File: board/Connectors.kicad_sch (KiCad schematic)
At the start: 17 parts, among them J10 SLOT 4, J11 SLOT 1, J12 SLOT 5, J13 SLOT 2, J14 SPI Device 0, J15 SPI Device 4, J16 SPI Device 1, J17 SPI Device 5, J18 Audio Jack, J19 SPI Device 2, J20 SPI Device 6, J21 SPI Device 3, J22 SPI Device 7, J23 SLOT 3, J24 VIA Port A, J25 SP720APP, J9 SLOT 0

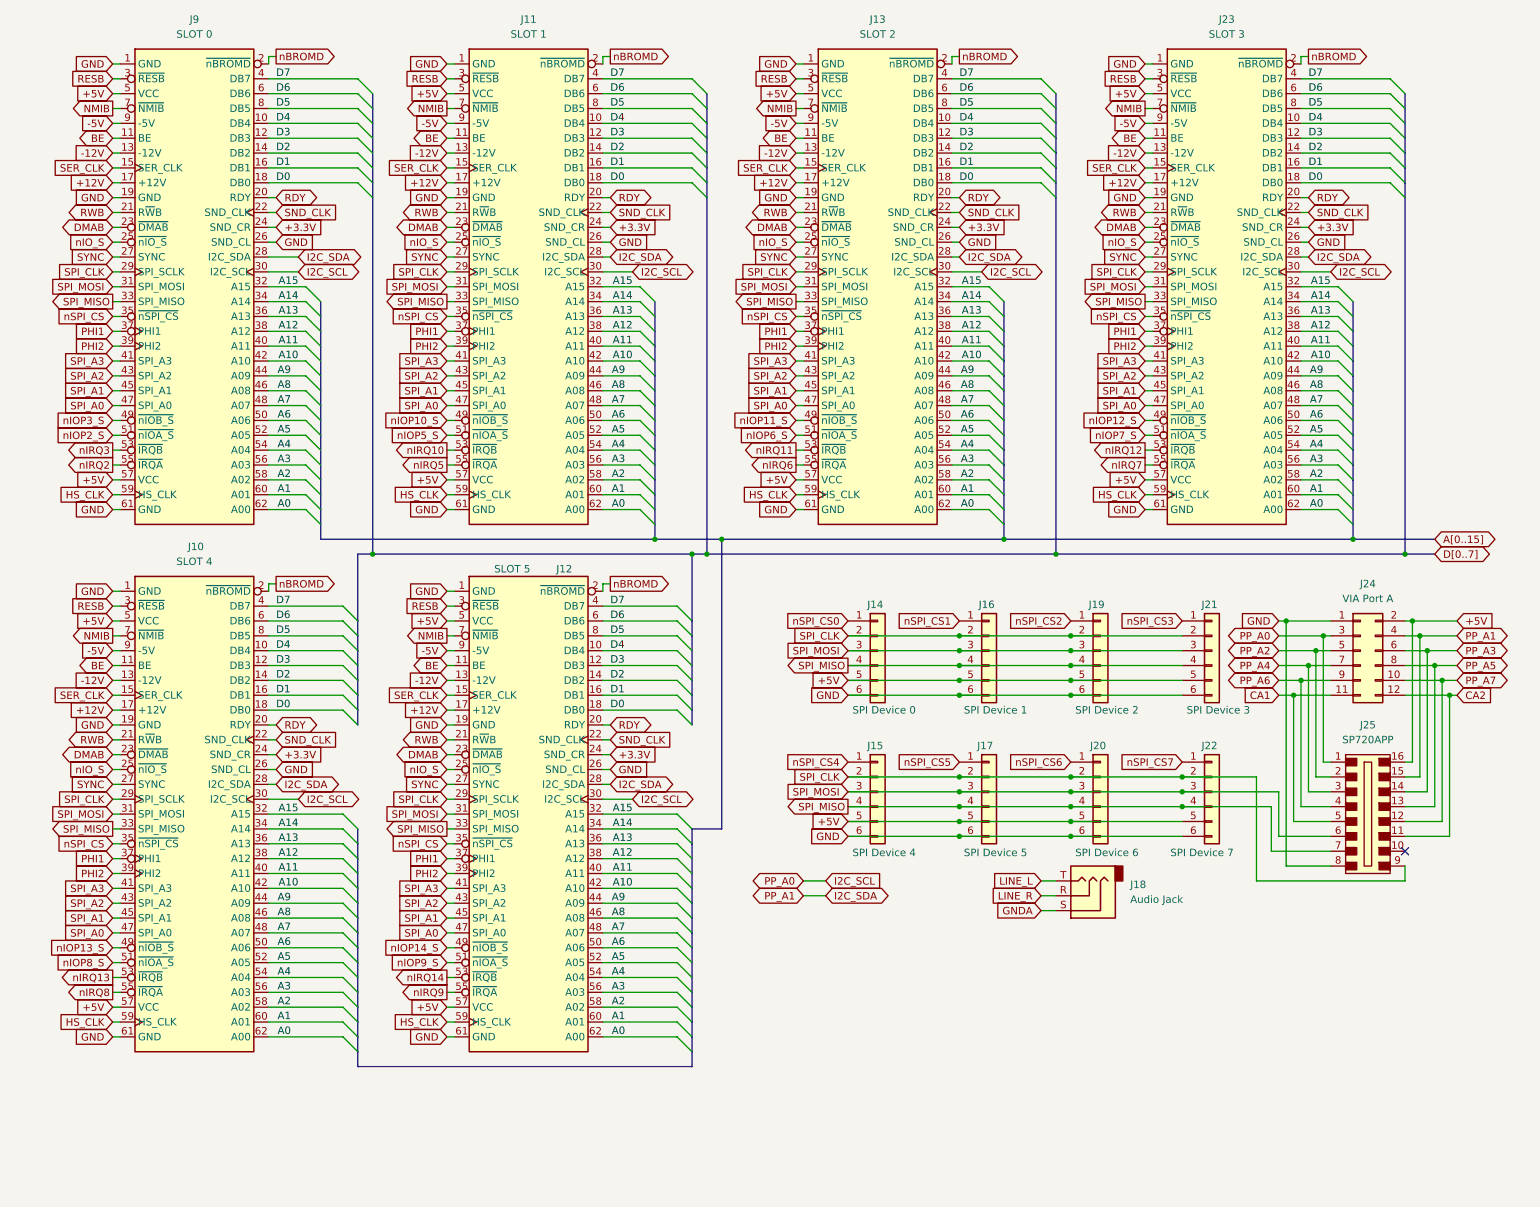
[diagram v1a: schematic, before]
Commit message: V2.0 rev 2.0D: clock stretching, OS ROM paging and review fixes
Bus timing:
- New GAL C (U88) generates PHI2/PHI1 and the 3.58 MHz sound clock from
  the 14.318 MHz master, replacing the U35 74F191 divider. J36 now selects
  7.16 or 3.58 MHz.
- Banked RAM, banked ROM and slot I/O ($FF20-$FFEF) get one extra PHI2-low
  period plus 0-3 extra PHI2-high periods set in $FFF5 (GAL D). This
  replaces the on-board RDY wait generator; cards can still pull RDY.
- Write strobes are now hold-time safe: PHI1 comes straight from GAL C
  and RWB_M straight from GAL B2.

Review fixes:
- OS ROM chip enable from a single-level decode, output enable from
  GAL B1; -55 part specified. Full 4K OS ROM paging via GAL G.
- Vector RAM writes only during PHI2; $FFF0-$FFFF no longer slowed.
- YM2151 /WR on RWB_M. U62 removed. RB0-RB7 pull-ups (RN5).
- Slot clocks driven through U56 and U34 with 33R series resistors.
- J38 enables in-system flashing of the banked ROMs.
- W65C22S/W65C51N, AS6C4008, DS1813-5 and CY7C192-25 values; R4 1k.
- J7 pin 8 no longer +5V; +5VA renamed +5VSB; serial handshake loop.
- Sheet titles and revisions, slot symbol pin fixes, and project symbol
  and footprint libraries so the project opens on another machine.

Co-Authored-By: Claude Opus 5.5 <noreply@anthropic.com>
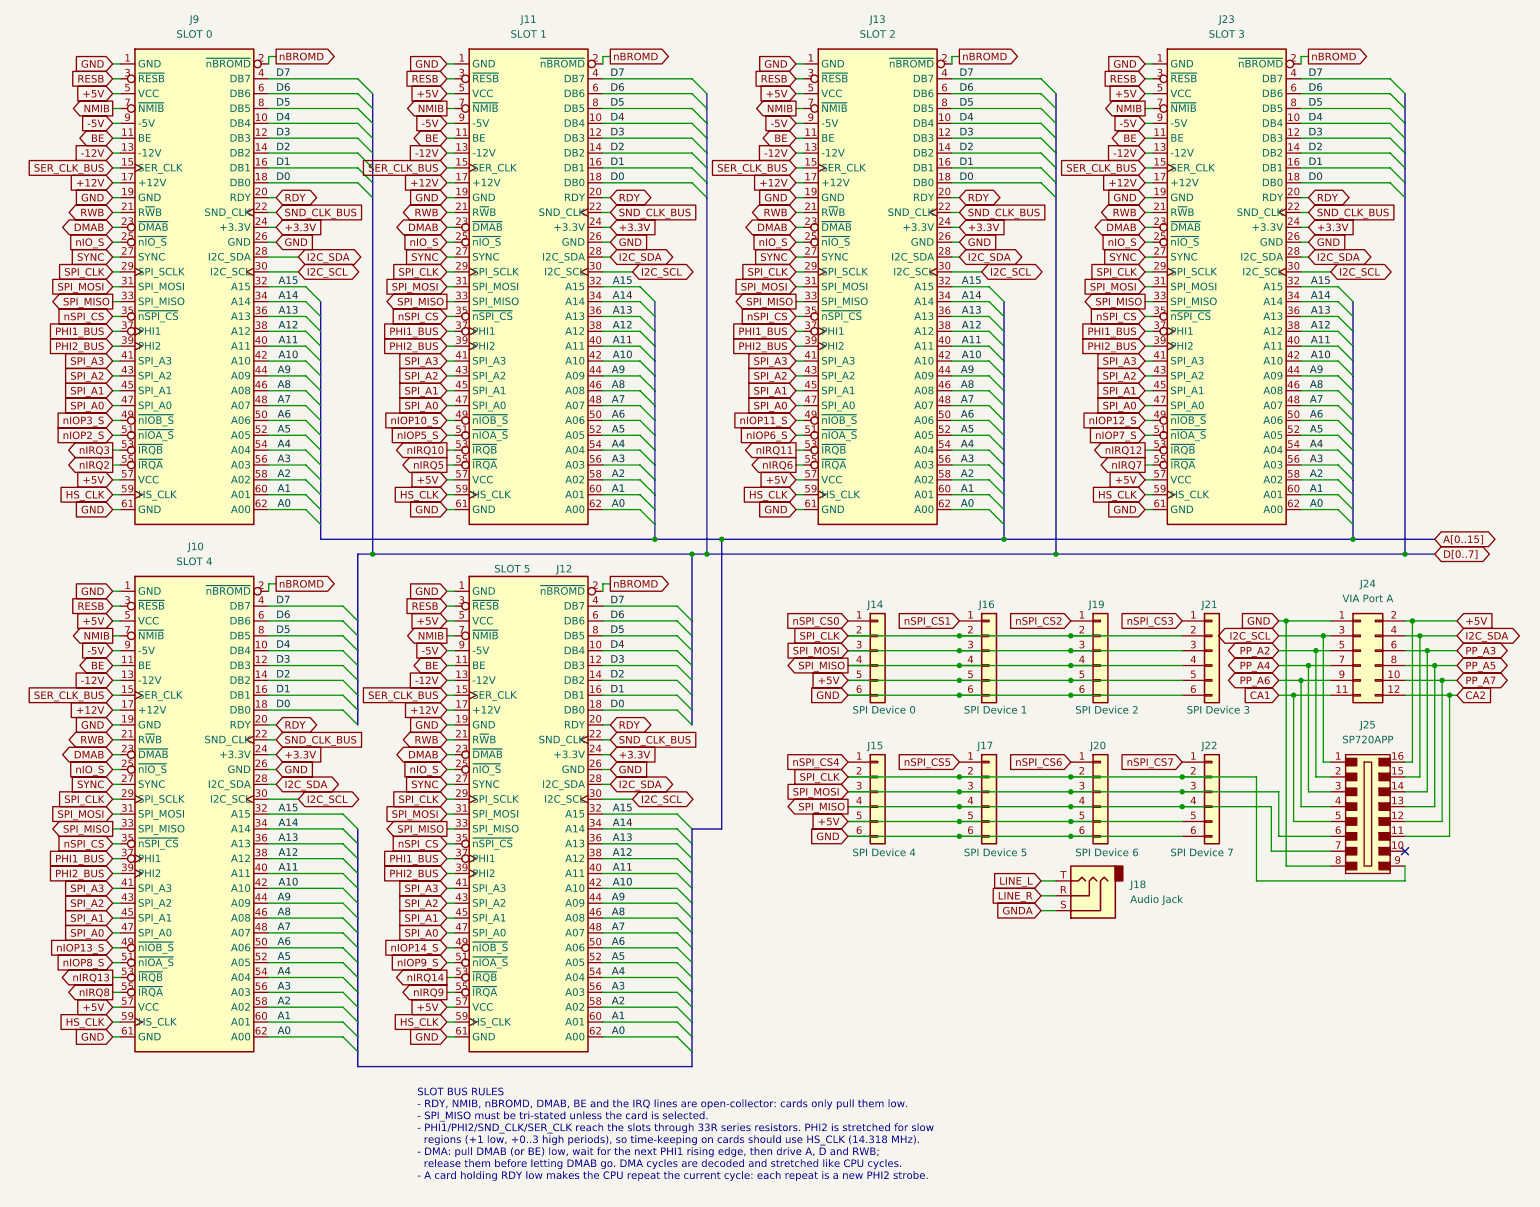
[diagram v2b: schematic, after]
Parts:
- J10, J11, J12, J13, J23, J9: footprint PC Edge:TE_7-5530843-0 -> Hydra16:TE_7-5530843-0; symbol Connector:Bus_Hydra_8bit -> Hydra16:Bus_Hydra_8bit
- J25: symbol dk_Sockets-for-ICs-Transistors:A_16-LC-TT -> Hydra16:A_16-LC-TT
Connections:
- net PHI1 renamed PHI1_BUS
- net PHI2 renamed PHI2_BUS
- net SER_CLK renamed SER_CLK_BUS
- net SND_CLK renamed SND_CLK_BUS
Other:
- note added: "SLOT BUS RULES - RDY, NMIB, nBROMD, DMAB, BE and the IRQ lines are open-collector: cards only pull them low. - SPI_MISO must be tri-stated unless the card is selected. - PHI1/PHI2/SND_CLK/SER_CLK reach the slots through 33R series resistors. PHI2 is stretched for slow regions (+1 low, +0..3 high periods), so time-keeping on cards should use HS_CLK (14.318 MHz). - DMA: pull DMAB (or BE) low, wait 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"
- title: ZeroPage $00/$01 Mirror Memory and RAM/ROM Bank Logic -> Expansion Slots, SPI Headers and Port A
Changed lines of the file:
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@@
 	(generator "eeschema")
 	(generator_version "9.0")
-	(paper "USLetter")
+	(paper "USLedger")
 	(title_block
-		(title "ZeroPage $00/$01 Mirror Memory and RAM/ROM Bank Logic")
-		(date "2026-01-28")
-		(rev "2.0B")
+		(title "Expansion Slots, SPI Headers and Port A")
+		(date "2026-10-06")
+		(rev "2.0D")
 		(company "Data Tuning")
 		(comment 1 "Hydra 16")
@@
 	(wire
 		(pts
-			(xy 144.78 165.1) (xy 148.59 165.1)
-		)
-		(stroke
-			(width 0)
-			(type default)
-		)
-	)
-	(wire
-		(pts
 			(xy 229.87 71.12) (xy 236.22 71.12)
 		)
@@
 	(wire
 		(pts
-			(xy 144.78 162.56) (xy 148.59 162.56)
-		)
-		(stroke
-			(width 0)
-			(type default)
-		)
-	)
-	(wire
-		(pts
 			(xy 83.82 115.57) (xy 85.09 115.57)
 		)
@@
 		)
 	)
-	(global_label "SER_CLK"
+	(global_label "SER_CLK_BUS"
 		(shape input)
 		(at 26.67 130.81 180)
@@
 		)
 	)
-	(global_label "PP_A1"
-		(shape bidirectional)
-		(at 144.78 165.1 180)
-		(fields_autoplaced yes)
-		(effects
-			(font
-				(size 1.27 1.27)
-			)
-			(justify right)
-		)
-		(property "Intersheetrefs" "${INTERSHEET_REFS}"
-			(at 134.8778 165.1 0)
-			(effects
-				(font
-					(size 1.27 1.27)
-				)
-				(justify right)
-				(hide yes)
-			)
-		)
-	)
 	(global_label "nIO_S"
 		(shape input)
@@
 		)
 	)
-	(global_label "SND_CLK"
+	(global_label "SND_CLK_BUS"
 		(shape input)
 		(at 54.61 138.43 0)
@@
 		)
 	)
-	(global_label "PHI1"
+	(global_label "PHI1_BUS"
 		(shape input)
 		(at 143.51 68.58 180)
@@
 		)
 	)
-	(global_label "SND_CLK"
+	(global_label "SND_CLK_BUS"
 		(shape input)
 		(at 171.45 48.26 0)
@@
 		)
 	)
-	(global_label "SER_CLK"
+	(global_label "SER_CLK_BUS"
 		(shape input)
 		(at 143.51 40.64 180)
@@
 		)
 	)
-	(global_label "SER_CLK"
+	(global_label "SER_CLK_BUS"
 		(shape input)
 		(at 203.2 40.64 180)
@@
 		)
 	)
-	(global_label "PHI2"
+	(global_label "PHI2_BUS"
 		(shape input)
 		(at 83.82 71.12 180)
@@
 		)
 	)
-	(global_label "PHI2"
+	(global_label "PHI2_BUS"
 		(shape input)
 		(at 83.82 161.29 180)
@@
 		)
 	)
-	(global_label "PHI2"
+	(global_label "PHI2_BUS"
 		(shape input)
 		(at 143.51 71.12 180)
@@
 		)
 	)
-	(global_label "SER_CLK"
+	(global_label "SER_CLK_BUS"
 		(shape input)
 		(at 26.67 40.64 180)
@@
 		)
 	)
-	(global_label "PHI1"
+	(global_label "PHI1_BUS"
 		(shape input)
 		(at 83.82 68.58 180)
@@
 		)
 	)
-	(global_label "SND_CLK"
+	(global_label "SND_CLK_BUS"
 		(shape input)
 		(at 231.14 48.26 0)
@@
 		)
 	)
-	(global_label "SND_CLK"
+	(global_label "SND_CLK_BUS"
 		(shape input)
 		(at 111.76 138.43 0)
@@
 		)
 	)
-	(global_label "PHI2"
+	(global_label "PHI2_BUS"
 		(shape input)
 		(at 203.2 71.12 180)
@@
 		)
 	)
-	(global_label "PHI1"
+	(global_label "PHI1_BUS"
 		(shape input)
 		(at 26.67 68.58 180)
@@
 		)
 	)
-	(global_label "PHI2"
+	(global_label "PHI2_BUS"
 		(shape input)
 		(at 26.67 161.29 180)
@@
 		)
 	)
-	(global_label "PP_A0"
+	(global_label "I2C_SCL"
 		(shape bidirectional)
 		(at 226.06 120.65 180)
@@
 		)
 	)
-	(global_label "PHI1"
+	(global_label "PHI1_BUS"
 		(shape input)
 		(at 203.2 68.58 180)
@@
 		)
 	)
-	(global_label "PHI2"
+	(global_label "PHI2_BUS"
 		(shape input)
 		(at 26.67 71.12 180)
@@
 		)
 	)
-	(global_label "PHI1"
+	(global_label "PHI1_BUS"
 		(shape input)
 		(at 26.67 158.75 180)
@@
 		)
 	)
-	(global_label "PP_A0"
-		(shape bidirectional)
-		(at 144.78 162.56 180)
-		(fields_autoplaced yes)
-		(effects
-			(font
-				(size 1.27 1.27)
-			)
-			(justify right)
-		)
-		(property "Intersheetrefs" "${INTERSHEET_REFS}"
-			(at 134.8778 162.56 0)
-			(effects
-				(font
-					(size 1.27 1.27)
-				)
-				(justify right)
-				(hide yes)
-			)
-		)
-	)
 	(global_label "SPI_CLK"
 		(shape input)
@@
 		)
 	)
-	(global_label "I2C_SDA"
-		(shape bidirectional)
-		(at 148.59 165.1 0)
-		(fields_autoplaced yes)
-		(effects
-			(font
-				(size 1.27 1.27)
-			)
-			(justify left)
-		)
-		(property "Intersheetrefs" "${INTERSHEET_REFS}"
-			(at 160.3065 165.1 0)
-			(effects
-				(font
-					(size 1.27 1.27)
-				)
-				(justify left)
-				(hide yes)
-			)
-		)
-	)
 	(global_label "nIOP13_S"
 		(shape input)
@@
 		)
 	)
-	(global_label "SND_CLK"
+	(global_label "SND_CLK_BUS"
 		(shape input)
 		(at 111.76 48.26 0)
@@
 		)
 	)
-	(global_label "PP_A1"
+	(global_label "I2C_SDA"
 		(shape bidirectional)
 		(at 256.54 120.65 0)
@@
 		)
 	)
-	(global_label "SER_CLK"
+	(global_label "SER_CLK_BUS"
 		(shape input)
 		(at 83.82 130.81 180)
@@
 		)
 	)
-	(global_label "SER_CLK"
+	(global_label "SER_CLK_BUS"
 		(shape input)
 		(at 83.82 40.64 180)
@@
 		)
 	)
-	(global_label "SND_CLK"
+	(global_label "SND_CLK_BUS"
 		(shape input)
 		(at 54.61 48.26 0)
@@
 		)
 	)
-	(global_label "PHI1"
+	(global_label "PHI1_BUS"
 		(shape input)
 		(at 83.82 158.75 180)
@@
 		)
 	)
-	(global_label "I2C_SCL"
-		(shape input)
-		(at 148.59 162.56 0)
-		(fields_autoplaced yes)
-		(effects
-			(font
-				(size 1.27 1.27)
-			)
-			(justify left)
-		)
-		(property "Intersheetrefs" "${INTERSHEET_REFS}"
-			(at 159.1347 162.56 0)
-			(effects
-				(font
-					(size 1.27 1.27)
-				)
-				(justify left)
-				(hide yes)
-			)
-		)
-	)
 	(global_label "SPI_A3"
 		(shape input)
@@
 	)
 	(symbol
-		(lib_id "Connector:Bus_Hydra_8bit")
+		(lib_id "Hydra16:Bus_Hydra_8bit")
 		(at 97.79 60.96 0)
 		(unit 1)
@@
 			)
 		)
-		(property "Footprint" "PC Edge:TE_7-5530843-0"
+		(property "Footprint" "Hydra16:TE_7-5530843-0"
 			(at 97.79 105.918 0)
 			(effects
@@
 	)
 	(symbol
-		(lib_name "Bus_Hydra_8bit_3")
-		(lib_id "Connector:Bus_Hydra_8bit")
+		(lib_id "Hydra16:Bus_Hydra_8bit")
 		(at 40.64 151.13 0)
 		(unit 1)
@@
 			)
 		)
-		(property "Footprint" "PC Edge:TE_7-5530843-0"
+		(property "Footprint" "Hydra16:TE_7-5530843-0"
 			(at 40.64 196.088 0)
 			(effects
@@
 	)
 	(symbol
-		(lib_name "Bus_Hydra_8bit_1")
-		(lib_id "Connector:Bus_Hydra_8bit")
+		(lib_id "Hydra16:Bus_Hydra_8bit")
 		(at 40.64 60.96 0)
 		(unit 1)
@@
 			)
 		)
-		(property "Footprint" "PC Edge:TE_7-5530843-0"
+		(property "Footprint" "Hydra16:TE_7-5530843-0"
 			(at 40.64 105.918 0)
 			(effects
@@
 	)
 	(symbol
-		(lib_name "Bus_Hydra_8bit_5")
-		(lib_id "Connector:Bus_Hydra_8bit")
+		(lib_id "Hydra16:Bus_Hydra_8bit")
 		(at 157.48 60.96 0)
 		(unit 1)
@@
 			)
 		)
-		(property "Footprint" "PC Edge:TE_7-5530843-0"
+		(property "Footprint" "Hydra16:TE_7-5530843-0"
 			(at 157.48 105.918 0)
 			(effects
@@
 	)
 	(symbol
-		(lib_name "Bus_Hydra_8bit_4")
-		(lib_id "Connector:Bus_Hydra_8bit")
+		(lib_id "Hydra16:Bus_Hydra_8bit")
 		(at 217.17 60.96 0)
 		(unit 1)
@@
 			)
 		)
-		(property "Footprint" "PC Edge:TE_7-5530843-0"
+		(property "Footprint" "Hydra16:TE_7-5530843-0"
 			(at 217.17 105.918 0)
 			(effects
@@
 	)
 	(symbol
-		(lib_name "Bus_Hydra_8bit_2")
-		(lib_id "Connector:Bus_Hydra_8bit")
+		(lib_id "Hydra16:Bus_Hydra_8bit")
 		(at 97.79 151.13 0)
 		(unit 1)
@@
 			)
 		)
-		(property "Footprint" "PC Edge:TE_7-5530843-0"
+		(property "Footprint" "Hydra16:TE_7-5530843-0"
 			(at 97.79 196.088 0)
 			(effects
@@
 	)
 	(symbol
-		(lib_id "dk_Sockets-for-ICs-Transistors:A_16-LC-TT")
+		(lib_id "Hydra16:A_16-LC-TT")
 		(at 241.3 151.13 0)
 		(unit 1)
@@
 		)
 	)
+	(text "SLOT BUS RULES\n- RDY, NMIB, nBROMD, DMAB, BE and the IRQ lines are open-collector: cards only pull them low.\n- SPI_MISO must be tri-stated unless the card is selected.\n- PHI1/PHI2/SND_CLK/SER_CLK reach the slots through 33R series resistors. PHI2 is stretched for slow\n  regions (+1 low, +0..3 high periods), so time-keeping on cards should use HS_CLK (14.318 MHz).\n- DMA: pull DMAB (or BE) low, wait for the next PHI1 rising edge, then drive A, D and RWB;\n  release them before letting DMAB go. DMA cycles are decoded and stretched like CPU cycles.\n- A card holding RDY low makes the CPU repeat the current cycle: each repeat is a new PHI2 strobe."
+		(exclude_from_sim no)
+		(at 78.74 198.12 0)
+		(effects
+			(font
+				(size 1.27 1.27)
+			)
+			(justify left top)
+		)
+	)

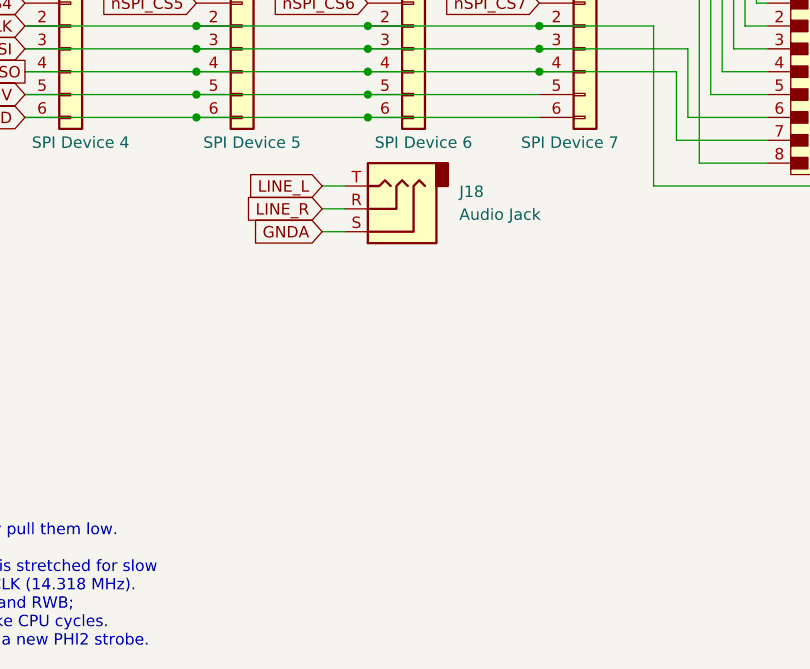
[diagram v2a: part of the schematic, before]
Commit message: V2.0: split Support sheet, add stereo amplifier and on-board speakers
Support sheet reorganized (connectivity unchanged):
- Support.kicad_sch renamed to Power: ATX, front panel, reset, soft power, -5V
- Oscillators and their parts moved to Clocks (now US Ledger)
- Sound-chip decoupling and line-out parts moved to Sound
- VIA CB1/CB2/SPI pull-ups moved to Connectors
- Also includes minor schematic edits made before the reorganization

Audio output rework (Sound, now A3):
- U89 TDA2822M stereo amplifier on 9 V from U90 L7809 (fed by +12V)
- RV1 dual 10k log volume pot behind R26/R27 220k attenuators
- J18 moved from Connectors and now uses the switched TRS symbol:
  a plug lifts T/R off TN/RN and mutes the on-board speakers
- LS1/LS2 8 ohm mini speakers through R30/R31 (15R 0.5 W)
- New footprint Speaker_D32mm_P15.24mm_P17.50mm (two pad pairs, fits
  Adafruit 1898 or Kitronik 3316)
- J39 line-out header (LINE_L, LINE_R, GNDA)
- R18 stays the single GNDA-GND tie, to sit at U89 pin 4
- TDA2822M symbol added to hydra16.kicad_sym

Co-Authored-By: Claude Opus 5.5 <noreply@anthropic.com>
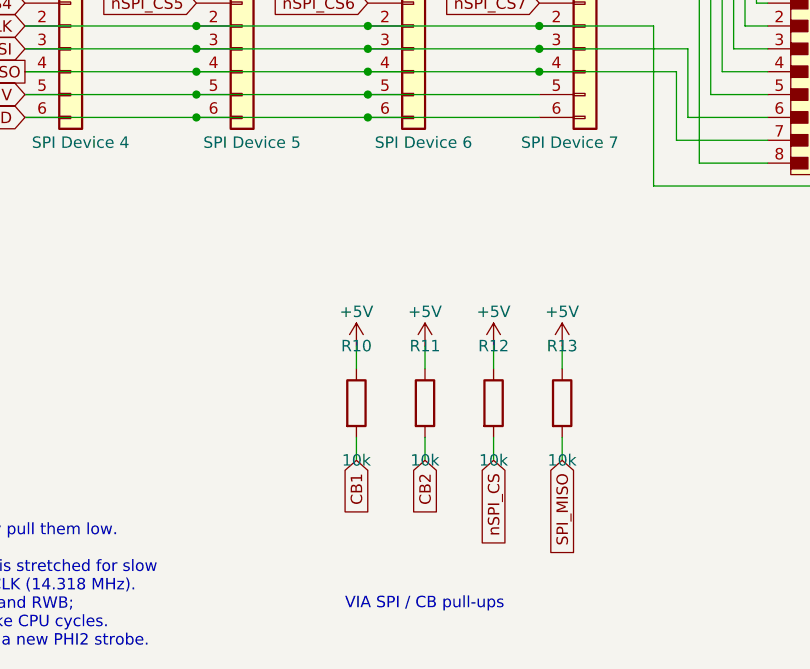
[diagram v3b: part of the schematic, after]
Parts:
- removed J18: Audio Jack, Connector_Audio:Jack_3.5mm_CUI_SJ1-3525N_Horizontal, symbol Connector_Audio:AudioJack3
- added R10, R11, R12, R13: 10k, Resistor_THT:R_Axial_DIN0204_L3.6mm_D1.6mm_P5.08mm_Horizontal, symbol Device:R
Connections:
- net +5V: now also R10.1, R11.1, R12.1, R13.1
- net SPI_MISO: now also R13.2
- net nSPI_CS: now also R12.2
- new net CB1: R10.2
- new net CB2: R11.2
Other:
- note added: "VIA SPI / CB pull-ups"
